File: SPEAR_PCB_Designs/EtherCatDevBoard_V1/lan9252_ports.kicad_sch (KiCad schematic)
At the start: 44 parts, among them J5 SM04B-GHS-TB, J6 SM04B-GHS-TB, T1 H1102NLT, T2 H1102NLT, U5 24FC512-I/SN

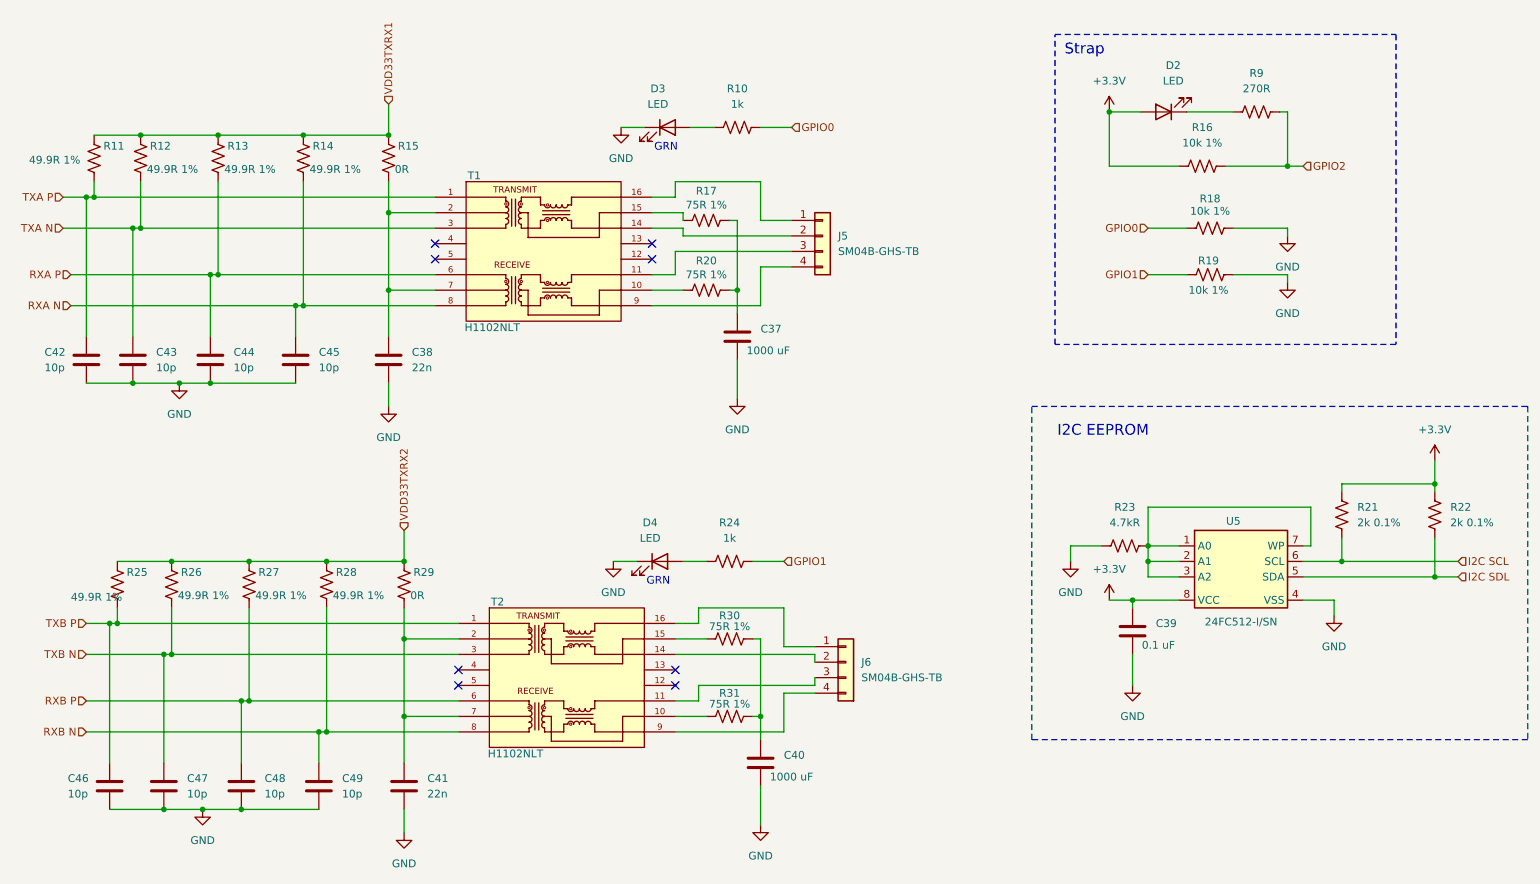
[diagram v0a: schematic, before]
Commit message: Continued work on the EtherCAT microcontroller dev. board. Not complete yet.
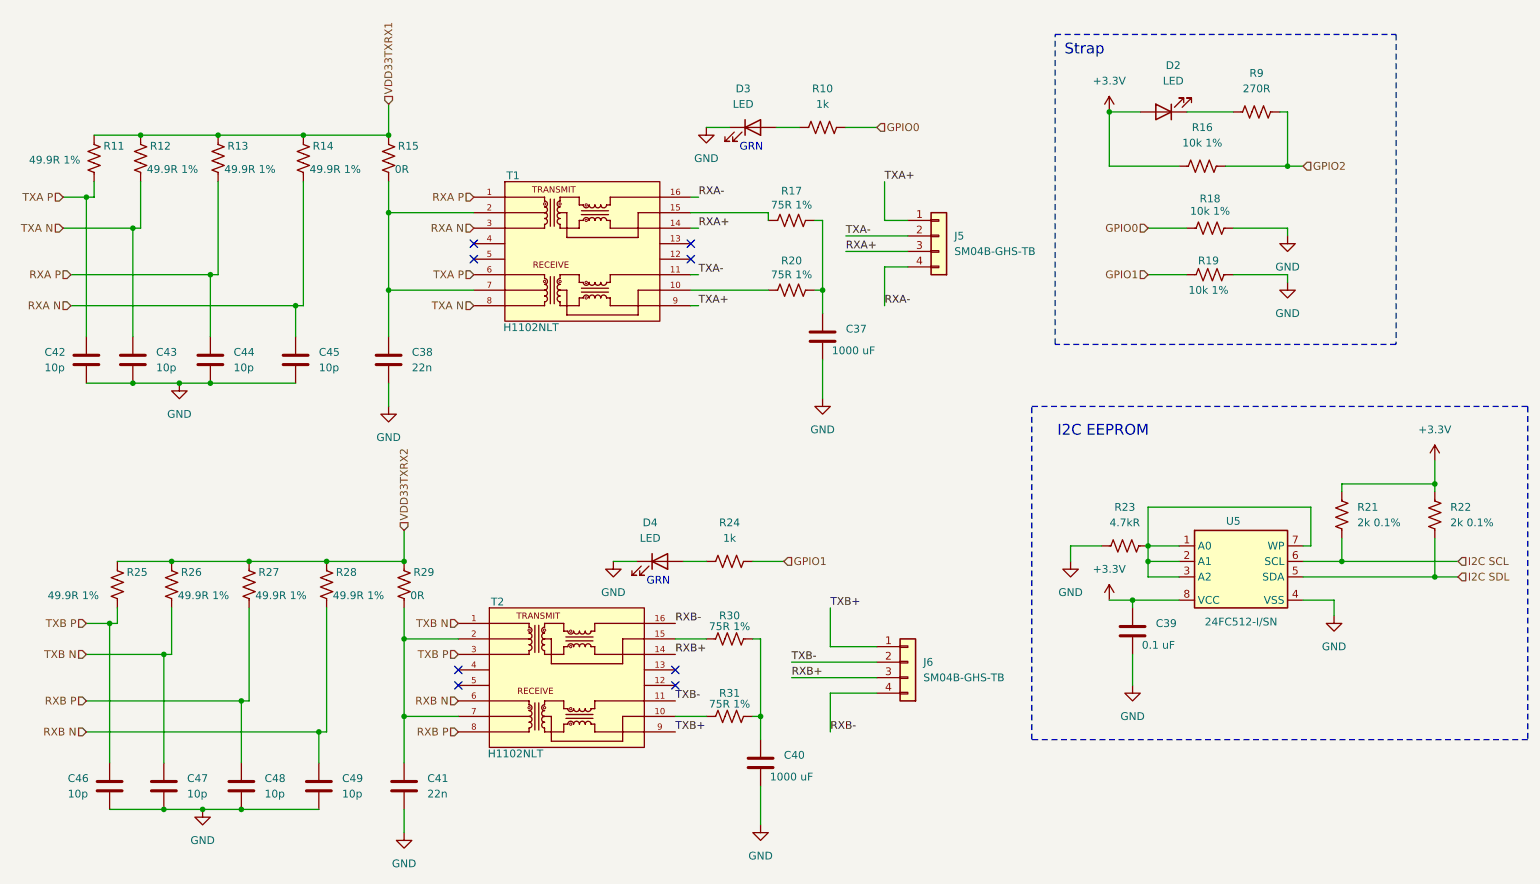
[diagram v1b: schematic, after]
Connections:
- net RXA N: now also T1.3; no longer T1.8
- net RXA P: now also T1.1; no longer T1.6
- net RXB N: now also T2.6; no longer T2.8
- net RXB P: now also T2.8; no longer T2.6
- net TXA N: now also T1.8; no longer T1.3
- net TXA P: now also T1.6; no longer T1.1
- net TXB N: now also T2.1; no longer T2.3
- net TXB P: now also T2.3; no longer T2.1
- net RXA+: now reaches J5.3 (Pin_3)
- net RXA+: now also T1.14; no longer T1.11
- net TXA-: now reaches J5.2 (Pin_2)
- net TXA-: now also T1.11; no longer T1.14
- net RXA-: now reaches T1.16
- net RXA-: now also J5.4 (Pin_4); no longer J5.1 (Pin_1)
- net TXA+: now reaches T1.9
- net TXA+: now also J5.1 (Pin_1); no longer J5.4 (Pin_4)
- net RXB+: now reaches J6.3 (Pin_3)
- net RXB+: now also T2.14; no longer T2.11
- net TXB-: now reaches J6.2 (Pin_2)
- net TXB-: now also T2.11; no longer T2.14
- net RXB-: now reaches T2.16
- net RXB-: now also J6.4 (Pin_4); no longer J6.1 (Pin_1)
- net TXB+: now reaches T2.9
- net TXB+: now also J6.1 (Pin_1); no longer J6.4 (Pin_4)
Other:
- moved on the sheet: C37, D3, J5, J6, R10, R17, R20, T1

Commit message: Henry's continued work on the EtherCAT microcontroller dev. board.
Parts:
- D2, D3, D4: footprint LED_SMD:LED_0402_1005Metric -> LED_SMD:LED_0603_1608Metric
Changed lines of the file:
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@@
 			)
 		)
-		(property "Footprint" "LED_SMD:LED_0402_1005Metric"
+		(property "Footprint" "LED_SMD:LED_0603_1608Metric"
 			(at 124.46 115.57 0)
 			(effects
@@
 			)
 		)
-		(property "Footprint" "LED_SMD:LED_0402_1005Metric"
+		(property "Footprint" "LED_SMD:LED_0603_1608Metric"
 			(at 207.01 41.91 0)
 			(effects
@@
 			)
 		)
-		(property "Footprint" "LED_SMD:LED_0402_1005Metric"
+		(property "Footprint" "LED_SMD:LED_0603_1608Metric"
 			(at 139.7 44.45 0)
 			(effects

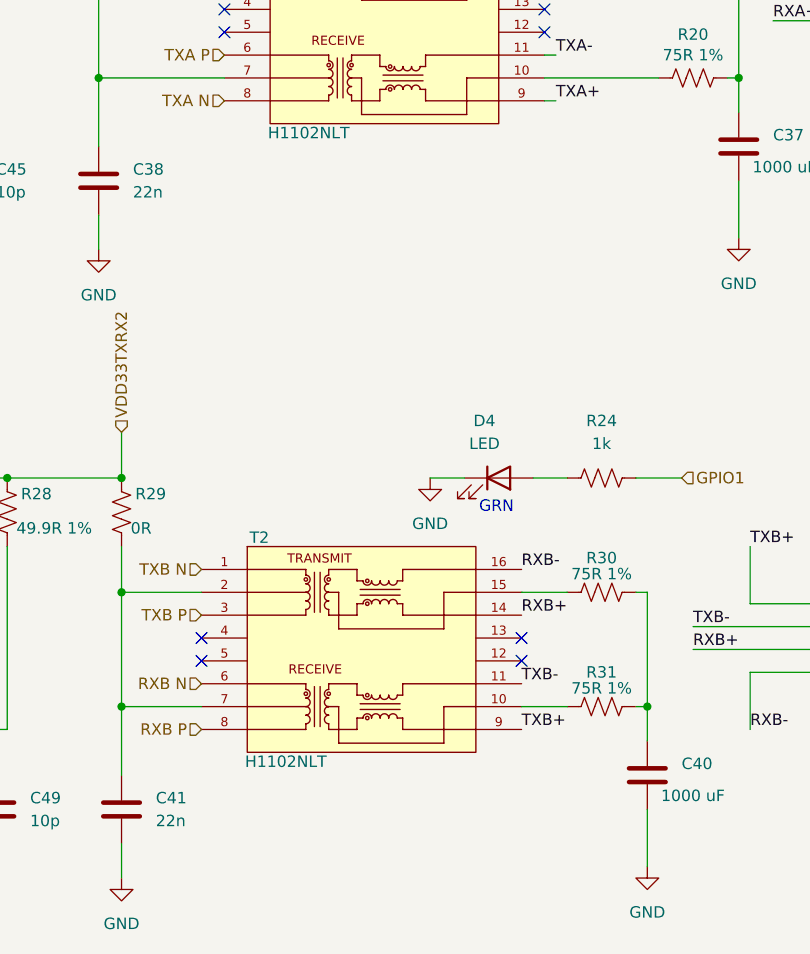
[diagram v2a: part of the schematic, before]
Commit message: Edited schematic to fix problems with Lan9252. Continued work on pcb layout.
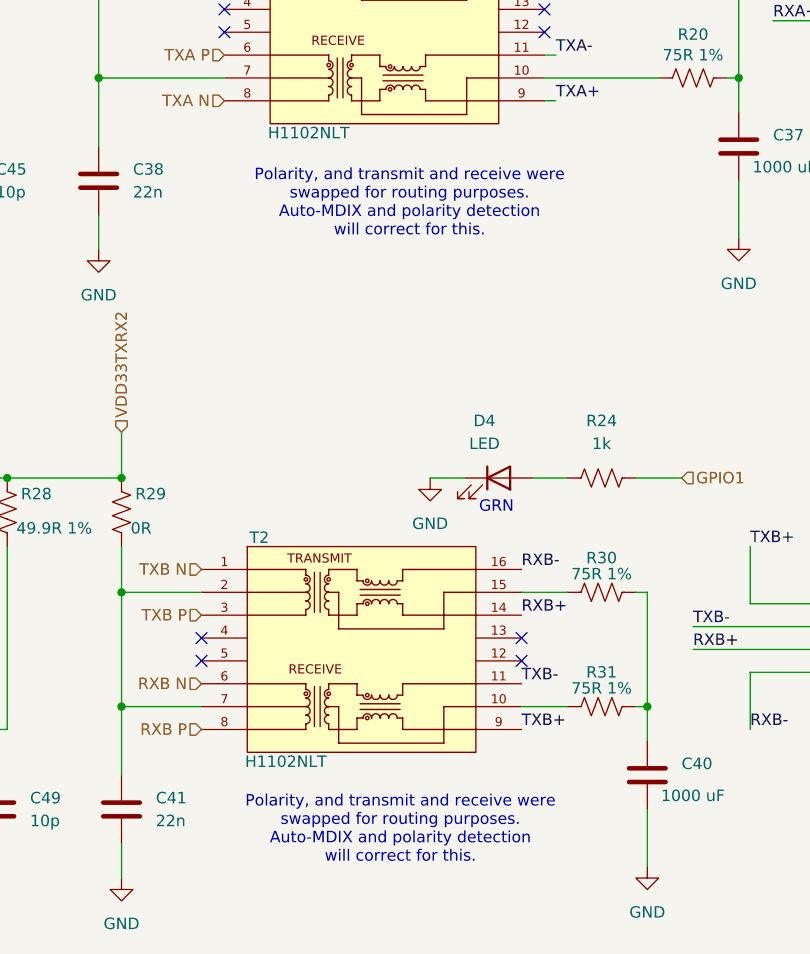
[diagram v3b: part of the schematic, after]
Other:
- note added: "Polarity, and transmit and receive were swapped for routing purposes. Auto-MDIX and polarity detection will correct for this."
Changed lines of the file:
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@@
+		)
+	)
+	(text "Polarity, and transmit and receive were\nswapped for routing purposes.\nAuto-MDIX and polarity detection \nwill correct for this."
+		(exclude_from_sim no)
+		(at 113.538 154.686 0)
+		(effects
+			(font
+				(size 1.27 1.27)
+			)
 		)
 	)
@@
 			)
 		)
+	)
+	(text "Polarity, and transmit and receive were\nswapped for routing purposes.\nAuto-MDIX and polarity detection \nwill correct for this."
+		(exclude_from_sim no)
+		(at 114.554 85.09 0)
+		(effects
+			(font
+				(size 1.27 1.27)
+			)
+		)

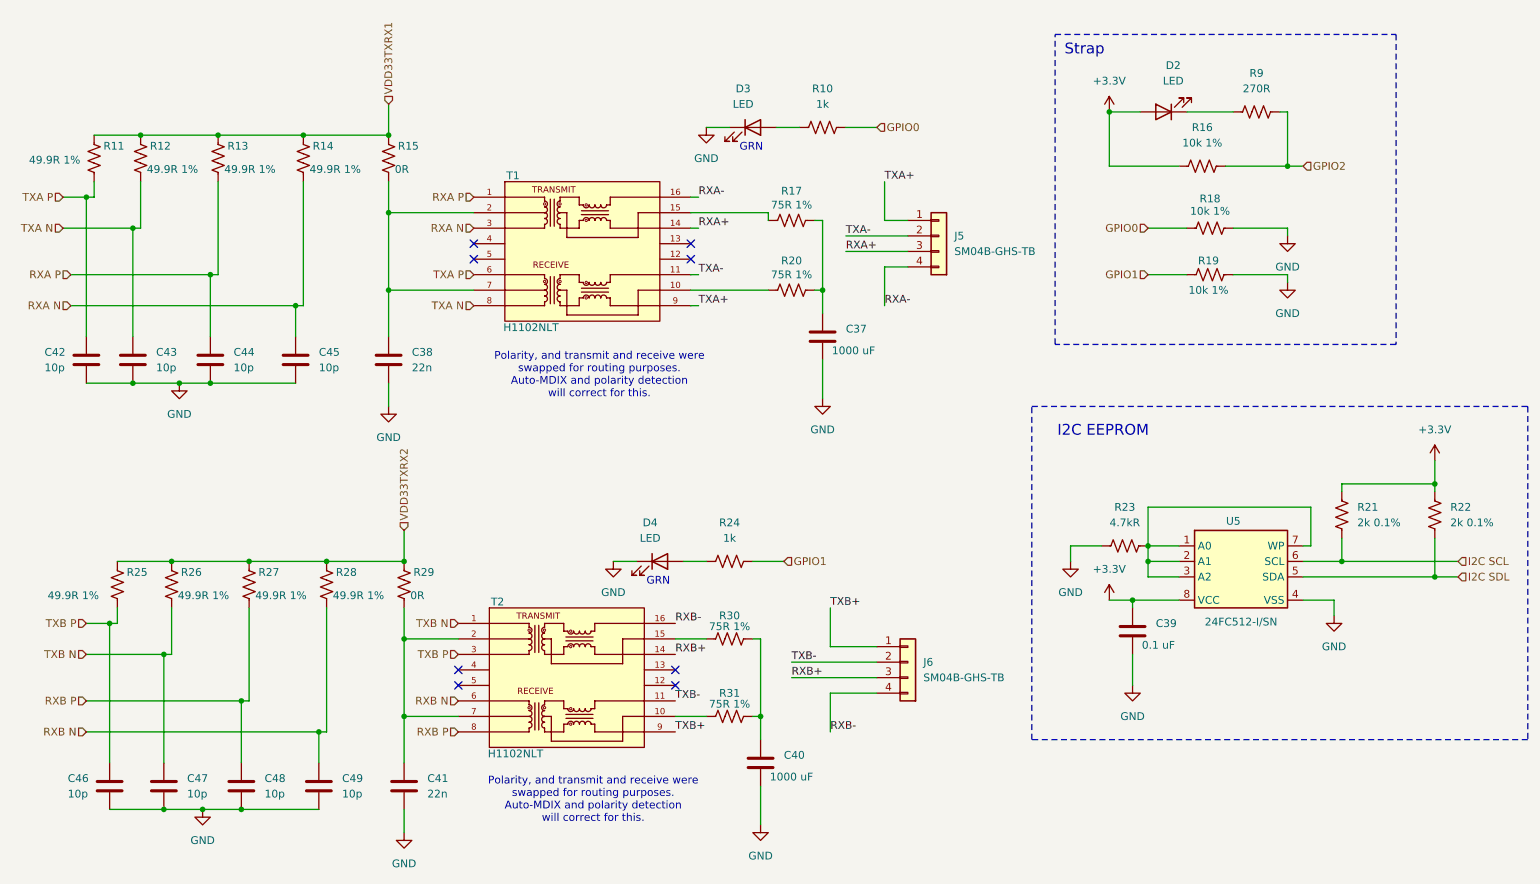
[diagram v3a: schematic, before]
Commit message: Started adding digikey part ID's to the EtherCAT microcontroller dev. board, but incomplete as of now.
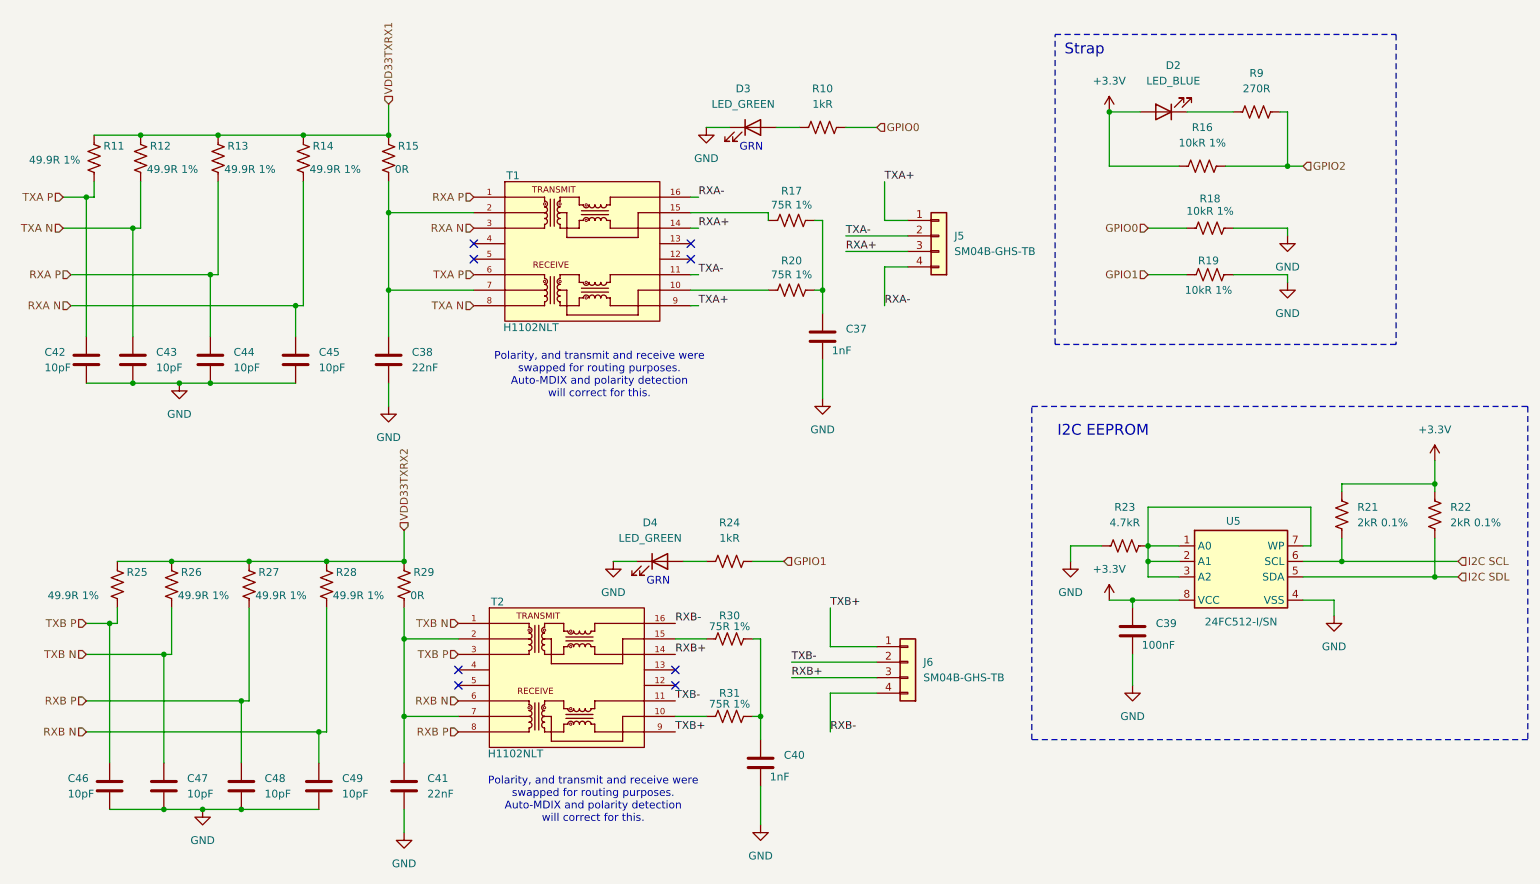
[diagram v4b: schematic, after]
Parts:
- C37, C40: value 1000 uF -> 1nF; DigiKey_Part_Number (none) -> 1276-1032-1-ND
- C38, C41: value 22n -> 22nF; DigiKey_Part_Number (none) -> 1276-1537-1-ND
- C39: value 0.1 uF -> 100nF; DigiKey_Part_Number (none) -> 1276-1043-1-ND
- C42, C43, C44, C45, C46, C47, C48, C49: value 10p -> 10pF; DigiKey_Part_Number (none) -> 1276-1139-1-ND
- D2: value LED -> LED_BLUE; DigiKey_Part_Number (none) -> 732-12013-1-ND
- D3, D4: value LED -> LED_GREEN; DigiKey_Part_Number (none) -> 732-12017-1-ND
- R10, R24: value 1k -> 1kR; DigiKey_Part_Number (none) -> 311-1.0KJRCT-ND
- R11, R12, R13, R14, R25, R26, R27, R28: DigiKey_Part_Number (none) -> 311-49.9LRCT-ND
- R15, R29: DigiKey_Part_Number (none) -> 311-0.0JRCT-ND
- R16, R18, R19: value 10k 1% -> 10kR 1%; DigiKey_Part_Number (none) -> 311-10.0KLRCT-ND
- R17, R20, R30, R31: DigiKey_Part_Number (none) -> 13-RC0402FR-1375RLCT-ND
- R21, R22: value 2k 0.1% -> 2kR 0.1%; DigiKey_Part_Number (none) -> YAG2303CT-ND
- R23: DigiKey_Part_Number (none) -> 311-4.7KJRCT-ND
- R9: DigiKey_Part_Number (none) -> 311-270LRCT-ND

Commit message: Finished etherCAT microcontroller dev board component selection. BOM is available. PCB layout incomplete.
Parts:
- J5, J6: DigiKey_Part_Number (none) -> 455-1566-1-ND
- T1, T2: DigiKey_Part_Number (none) -> 553-1532-1-ND
- U5: DigiKey_Part_Number (none) -> 24FC512-I/SN-ND
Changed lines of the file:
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@@
 			)
 		)
+		(property "DigiKey_Part_Number" "553-1532-1-ND"
+			(at 111.76 64.77 0)
+			(effects
+				(font
+					(size 1.27 1.27)
+				)
+				(hide yes)
+			)
+		)
 		(pin "2"
 		)
@@
 			)
 		)
+		(property "DigiKey_Part_Number" "553-1532-1-ND"
+			(at 109.22 134.62 0)
+			(effects
+				(font
+					(size 1.27 1.27)
+				)
+				(hide yes)
+			)
+		)
 		(pin "13"
 		)
@@
 			)
 		)
+		(property "DigiKey_Part_Number" "455-1566-1-ND"
+			(at 170.18 66.04 0)
+			(effects
+				(font
+					(size 1.27 1.27)
+				)
+				(hide yes)
+			)
+		)
 		(pin "1"
 		)
@@
 			)
 		)
+		(property "DigiKey_Part_Number" "24FC512-I/SN-ND"
+			(at 219.71 115.57 0)
+			(effects
+				(font
+					(size 1.27 1.27)
+				)
+				(hide yes)
+			)
+		)
 		(pin "6"
 		)
@@
 			(at 165.1 135.89 0)
 			(effects
+				(font
+					(size 1.27 1.27)
+				)
+				(hide yes)
+			)
+		)
+		(property "DigiKey_Part_Number" "455-1566-1-ND"
+			(at 165.1 135.89 0)
+			(effects
